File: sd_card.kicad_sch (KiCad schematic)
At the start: 19 parts, among them J1101 DM3AT-SF-PEJM5

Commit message: Update BOM, and fix MPU pinout
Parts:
- R1101, R1102, R1103, R1104, R1105, R1106, R1107, R1108, R1109: footprint Resistor_SMD:R_0201_0603Metric -> perfect_footprints:R_0201_0603Metric
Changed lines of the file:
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@@
 			)
 		)
-		(property "Footprint" "Resistor_SMD:R_0201_0603Metric"
+		(property "Footprint" "perfect_footprints:R_0201_0603Metric"
 			(at 114.3 140.462 90)
 			(effects
@@
 			)
 		)
-		(property "Footprint" "Resistor_SMD:R_0201_0603Metric"
+		(property "Footprint" "perfect_footprints:R_0201_0603Metric"
 			(at 114.3 135.382 90)
 			(effects
@@
 			)
 		)
-		(property "Footprint" "Resistor_SMD:R_0201_0603Metric"
+		(property "Footprint" "perfect_footprints:R_0201_0603Metric"
 			(at 114.3 145.542 90)
 			(effects
@@
 			)
 		)
-		(property "Footprint" "Resistor_SMD:R_0201_0603Metric"
+		(property "Footprint" "perfect_footprints:R_0201_0603Metric"
 			(at 125.222 120.65 90)
 			(effects
@@
 			)
 		)
-		(property "Footprint" "Resistor_SMD:R_0201_0603Metric"
+		(property "Footprint" "perfect_footprints:R_0201_0603Metric"
 			(at 114.3 127.762 90)
 			(effects
@@
 			)
 		)
-		(property "Footprint" "Resistor_SMD:R_0201_0603Metric"
+		(property "Footprint" "perfect_footprints:R_0201_0603Metric"
 			(at 114.3 143.002 90)
 			(effects
@@
 			)
 		)
-		(property "Footprint" "Resistor_SMD:R_0201_0603Metric"
+		(property "Footprint" "perfect_footprints:R_0201_0603Metric"
 			(at 135.128 154.94 90)
 			(effects
@@
 			)
 		)
-		(property "Footprint" "Resistor_SMD:R_0201_0603Metric"
+		(property "Footprint" "perfect_footprints:R_0201_0603Metric"
 			(at 114.3 130.302 90)
 			(effects
@@
 			)
 		)
-		(property "Footprint" "Resistor_SMD:R_0201_0603Metric"
+		(property "Footprint" "perfect_footprints:R_0201_0603Metric"
 			(at 114.3 125.222 90)
 			(effects

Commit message: Rework MPU power
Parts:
- added R1109: 10 kΩ, perfect_footprints:R_0201_0603Metric, symbol Device:R
- renumbered R1109 to R1110
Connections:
- net VDD_SD is gone; now on net VDD: C1101.1, D1105.1 (A1), J1101.4 (VDD)
- net at D1104.1 (A1), J1101.5 (CLK), R1104.2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: now also R1109.2
- new net VDD_SD_IO: R1109.1
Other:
- moved on the sheet: R1101, R1102, R1103, R1104, R1105, R1106, R1107, R1108

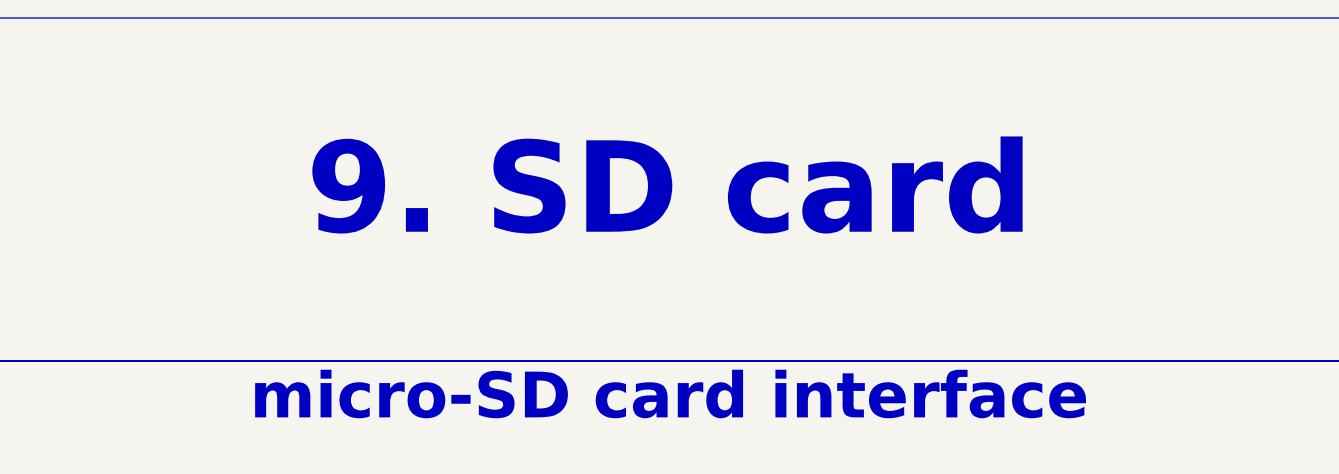
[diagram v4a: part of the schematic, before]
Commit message: Rework the schematics
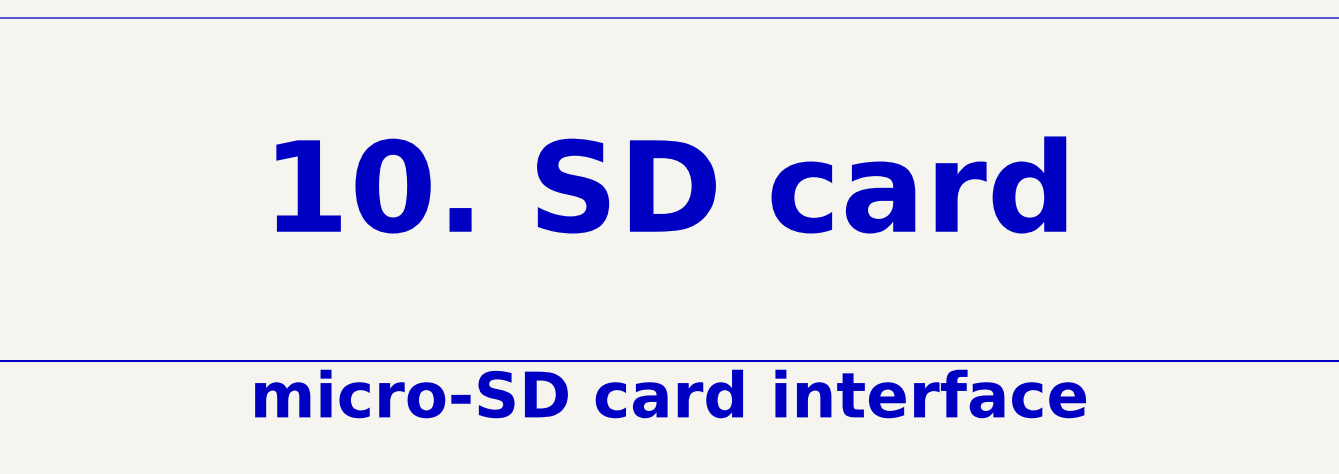
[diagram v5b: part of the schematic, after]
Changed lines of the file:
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@@
 	(title_block
 		(title "Linux SBC")
-		(date "2025-12-17")
+		(date "2025-12-19")
 		(rev "v1.0.0")
 	)
@@
 		)
 	)
-	(text_box "9. SD card"
+	(text_box "10. SD card"
 		(exclude_from_sim no)
 		(at 12.7 12.7 0)

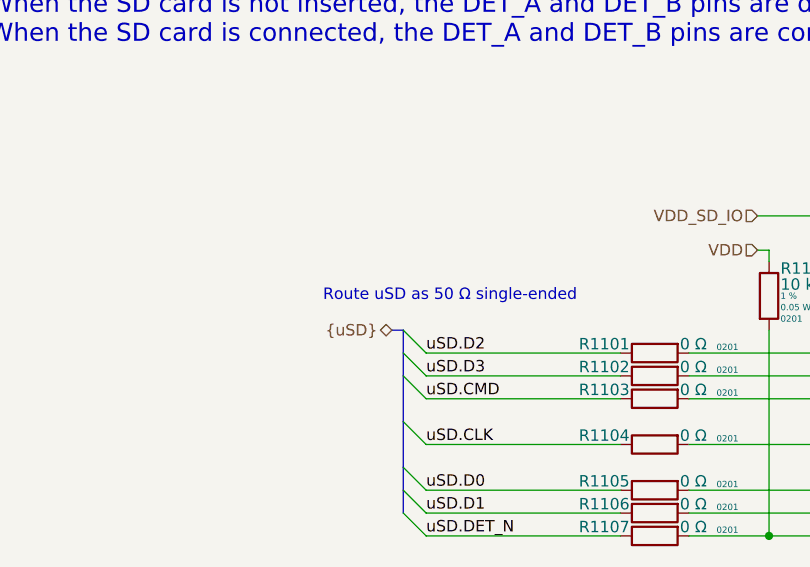
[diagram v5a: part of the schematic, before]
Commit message: Fix overflowing text
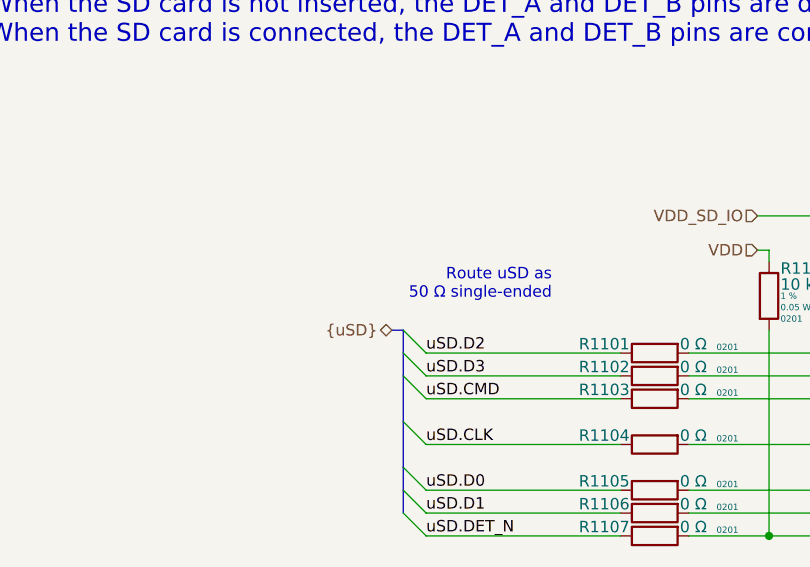
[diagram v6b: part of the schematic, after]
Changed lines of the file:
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@@
 		(rev "v1.0.0")
 	)
-	(text "Route uSD as 50 Ω single-ended"
+	(text "Route uSD as\n50 Ω single-ended"
 		(exclude_from_sim no)
-		(at 80.264 120.65 0)
+		(at 77.47 119.38 0)
 		(effects
 			(font

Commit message: Rework text boxes
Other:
- note added: "Notes"
- note added: "micro-SD card interface"
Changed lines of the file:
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@@
 		(rev "v1.0.0")
+	)
+	(rectangle
+		(start 12.7 50.8)
+		(end 406.4 251.46)
+		(stroke
+			(width 0)
+			(type default)
+		)
+		(fill
+			(type none)
+		)
+	)
+	(rectangle
+		(start 12.7 251.46)
+		(end 298.45 284.48)
+		(stroke
+			(width 0)
+			(type default)
+		)
+		(fill
+			(type none)
+		)
+	)
+	(text "Notes"
+		(exclude_from_sim no)
+		(at 13.97 254 0)
+		(effects
+			(font
+				(size 5.08 5.08)
+				(thickness 1.016)
+				(bold yes)
+			)
+			(justify left top)
+		)
+	)
+	(text "micro-SD card interface"
+		(exclude_from_sim no)
+		(at 13.97 53.34 0)
+		(effects
+			(font
+				(size 5.08 5.08)
+				(thickness 1.016)
+				(bold yes)
+			)
+			(justify left top)
+		)
 	)
 	(text "Route uSD as\n50 Ω single-ended"
@@
 		)
 	)
-	(text_box "micro-SD card interface"
-		(exclude_from_sim no)
-		(at 12.7 50.8 0)
-		(size 393.7 200.66)
-		(margins 0.9525 2 0.9525 0.9525)
-		(stroke
-			(width 0)
-			(type solid)
-		)
-		(fill
-			(type none)
-		)
-		(effects
-			(font
-				(size 5.08 5.08)
-				(thickness 1.016)
-				(bold yes)
-			)
-			(justify top)
-		)
-	)
-	(text_box "Notes"
-		(exclude_from_sim no)
-		(at 12.7 251.46 0)
-		(size 285.75 33.02)
-		(margins 0.9525 2 0.9525 0.9525)
-		(stroke
-			(width 0)
-			(type solid)
-		)
-		(fill
-			(type none)
-		)
-		(effects
-			(font
-				(size 5.08 5.08)
-				(thickness 1.016)
-				(bold yes)
-			)
-			(justify top)
-		)
-	)
